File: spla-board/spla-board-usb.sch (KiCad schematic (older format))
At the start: 22 parts, among them J1 USB_B_Micro, U2 FT2232H, U3 93LC66B, X1 O252012MEDH4MI

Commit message: schematic: Add Digikey and ManufacturerId fields to big components.
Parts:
- U2: Digikey (none) -> 768-1024-1-ND; Manufacturer Id (none) -> FT2232HL
- U3: Digikey (none) -> 93LC66B/SN-ND; Manufacturer Id (none) -> 93LC66B/SN
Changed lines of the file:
@@
 F 2 "Package_QFP:LQFP-64_10x10mm_P0.5mm" H 9950 5650 50  0001 C CNN
 F 3 "https://www.ftdichip.com/Support/Documents/DataSheets/ICs/DS_FT2232H.pdf" H 9950 5650 50  0001 C CNN
+F 4 "768-1024-1-ND" H 9950 5650 50  0001 C CNN "Digikey"
+F 5 "FT2232HL" H 9950 5650 50  0001 C CNN "Manufacturer Id"
 	1    9950 5650
 	1    0    0    -1
@@
 F 2 "Package_SO:SOIC-8_3.9x4.9mm_P1.27mm" H 5700 6550 50  0001 C CNN
 F 3 "http://ww1.microchip.com/downloads/en/DeviceDoc/20001749K.pdf" H 5700 6550 50  0001 C CNN
+F 4 "93LC66B/SN-ND" H 5700 6550 50  0001 C CNN "Digikey"
+F 5 "93LC66B/SN" H 5700 6550 50  0001 C CNN "Manufacturer Id"
 	1    5700 6550
 	1    0    0    -1

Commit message: schematic: Select LED part.
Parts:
- D3, D4: Digikey (none) -> 732-4986-1-ND; Manufacturer Id (none) -> 150080VS75000
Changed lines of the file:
@@
 F 2 "LED_SMD:LED_0805_2012Metric" H 12400 6700 50  0001 C CNN
 F 3 "~" H 12400 6700 50  0001 C CNN
+F 4 "732-4986-1-ND" H 12400 6700 50  0001 C CNN "Digikey"
+F 5 "150080VS75000" H 12400 6700 50  0001 C CNN "Manufacturer Id"
 	1    12400 6700
 	0    -1   -1   0
@@
 F 2 "LED_SMD:LED_0805_2012Metric" H 12400 5600 50  0001 C CNN
 F 3 "~" H 12400 5600 50  0001 C CNN
+F 4 "732-4986-1-ND" H 12400 5600 50  0001 C CNN "Digikey"
+F 5 "150080VS75000" H 12400 5600 50  0001 C CNN "Manufacturer Id"
 	1    12400 5600
 	0    -1   -1   0

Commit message: schematic: Add part numbers for USB and power jack.
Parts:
- J1: Digikey (none) -> 732-5960-1-ND; Manufacturer Id (none) -> 629105150521
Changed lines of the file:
@@
 F 2 "Connector_USB:USB_Micro-B_Wuerth_629105150521" H 2950 4800 50  0001 C CNN
 F 3 "~" H 2950 4800 50  0001 C CNN
+F 4 "732-5960-1-ND" H 2800 4850 50  0001 C CNN "Digikey"
+F 5 "629105150521" H 2800 4850 50  0001 C CNN "Manufacturer Id"
 	1    2800 4850
 	1    0    0    1

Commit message: schematic: Lower-case 'k' in resistors.
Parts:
- R2, R4, R5: value 10K -> 10k
- R3: value 2.2K -> 2.2k
- R6: value 12K -> 12k
- R7: value 1K -> 1k
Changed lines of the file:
@@
 P 6800 6850
 F 0 "R3" V 6595 6850 50  0000 C CNN
-F 1 "2.2K" V 6686 6850 50  0000 C CNN
+F 1 "2.2k" V 6686 6850 50  0000 C CNN
 F 2 "Resistor_SMD:R_0603_1608Metric" V 6840 6840 50  0001 C CNN
 F 3 "~" H 6800 6850 50  0001 C CNN
@@
 P 6400 5600
 F 0 "R2" H 6468 5646 50  0000 L CNN
-F 1 "10K" H 6468 5555 50  0000 L CNN
+F 1 "10k" H 6468 5555 50  0000 L CNN
 F 2 "Resistor_SMD:R_0603_1608Metric" V 6440 5590 50  0001 C CNN
 F 3 "~" H 6400 5600 50  0001 C CNN
@@
 P 6850 5600
 F 0 "R4" H 6918 5646 50  0000 L CNN
-F 1 "10K" H 6918 5555 50  0000 L CNN
+F 1 "10k" H 6918 5555 50  0000 L CNN
 F 2 "Resistor_SMD:R_0603_1608Metric" V 6890 5590 50  0001 C CNN
 F 3 "~" H 6850 5600 50  0001 C CNN
@@
 P 7250 5600
 F 0 "R5" H 7318 5646 50  0000 L CNN
-F 1 "10K" H 7318 5555 50  0000 L CNN
+F 1 "10k" H 7318 5555 50  0000 L CNN
 F 2 "Resistor_SMD:R_0603_1608Metric" V 7290 5590 50  0001 C CNN
 F 3 "~" H 7250 5600 50  0001 C CNN
@@
 P 7800 5250
 F 0 "R6" H 7868 5296 50  0000 L CNN
-F 1 "12K" H 7868 5205 50  0000 L CNN
+F 1 "12k" H 7868 5205 50  0000 L CNN
 F 2 "Resistor_SMD:R_0603_1608Metric" V 7840 5240 50  0001 C CNN
 F 3 "~" H 7800 5250 50  0001 C CNN
@@
 P 8300 5600
 F 0 "R7" H 8368 5646 50  0000 L CNN
-F 1 "1K" H 8368 5555 50  0000 L CNN
+F 1 "1k" H 8368 5555 50  0000 L CNN
 F 2 "Resistor_SMD:R_0603_1608Metric" V 8340 5590 50  0001 C CNN
 F 3 "~" H 8300 5600 50  0001 C CNN

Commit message: schematic/pcb: Swap oscillator for FOX924 equivalent.
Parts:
- X1: value O252012MEDH4MI -> FT5HNBPK12.0-T1; footprint Crystal:Crystal_SMD_2520-4Pin_2.5x2.0mm -> Crystal:Crystal_SMD_5032-4Pin_5.0x3.2mm; symbol SPLA:O252012MEDH4MI -> SPLA:FT5HNBPK12.0-T1; Digikey (none) -> 631-1068-1-ND; Manufacturer Id (none) -> FT5HNBPK12.0-T1
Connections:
- no-connect marks 7 -> 8
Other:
- note removed: "CMOS digital oscillator, rather than FTDI's crystal suggestion"
- moved on the sheet: C2
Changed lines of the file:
@@
 L Device:C_Small C2
 U 1 1 5E53DEA7
-P 6350 7600
-F 0 "C2" H 6465 7646 50  0000 L CNN
-F 1 "0.1uF" H 6465 7555 50  0000 L CNN
-F 2 "Capacitor_SMD:C_0603_1608Metric" H 6388 7450 50  0001 C CNN
-F 3 "~" H 6350 7600 50  0001 C CNN
-	1    6350 7600
+P 6350 7700
+F 0 "C2" H 6465 7746 50  0000 L CNN
+F 1 "0.1uF" H 6465 7655 50  0000 L CNN
+F 2 "Capacitor_SMD:C_0603_1608Metric" H 6388 7550 50  0001 C CNN
+F 3 "~" H 6350 7700 50  0001 C CNN
+	1    6350 7700
 	1    0    0    -1
 $EndComp
@@
 L power:GND #PWR0105
 U 1 1 5E58FEB5
-P 6350 7900
-F 0 "#PWR0105" H 6350 7650 50  0001 C CNN
-F 1 "GND" H 6355 7727 50  0000 C CNN
-F 2 "" H 6350 7900 50  0001 C CNN
-F 3 "" H 6350 7900 50  0001 C CNN
-	1    6350 7900
+P 6350 8000
+F 0 "#PWR0105" H 6350 7750 50  0001 C CNN
+F 1 "GND" H 6355 7827 50  0000 C CNN
+F 2 "" H 6350 8000 50  0001 C CNN
+F 3 "" H 6350 8000 50  0001 C CNN
+	1    6350 8000
 	1    0    0    -1
 $EndComp
@@
 L power:+3V3 #PWR0109
 U 1 1 5E649611
-P 7550 7350
-F 0 "#PWR0109" H 7550 7200 50  0001 C CNN
-F 1 "+3V3" H 7565 7523 50  0000 C CNN
-F 2 "" H 7550 7350 50  0001 C CNN
-F 3 "" H 7550 7350 50  0001 C CNN
-	1    7550 7350
+P 6350 7350
+F 0 "#PWR0109" H 6350 7200 50  0001 C CNN
+F 1 "+3V3" H 6365 7523 50  0000 C CNN
+F 2 "" H 6350 7350 50  0001 C CNN
+F 3 "" H 6350 7350 50  0001 C CNN
+	1    6350 7350
 	1    0    0    -1
 $EndComp
@@
 FIFO_SIWU
 $Comp
-L SPLA:O252012MEDH4MI X1
+L SPLA:FT5HNBPK12.0-T1 X1
 U 1 1 5FDCFC82
 P 7150 7800
+AR Path="/5FDCFC82" Ref="X1"  Part="1"
+AR Path="/5E4F712F/5FDCFC82" Ref="X1"  Part="1"
 F 0 "X1" H 6850 8050 50  0000 L CNN
-F 1 "O252012MEDH4MI" H 7150 7550 50  0000 C CNN
-F 2 "Crystal:Crystal_SMD_2520-4Pin_2.5x2.0mm" H 7200 7300 50  0001 C CNN
+F 1 "FT5HNBPK12.0-T1" H 7150 7550 50  0000 C CNN
+F 2 "Crystal:Crystal_SMD_5032-4Pin_5.0x3.2mm" H 7200 7300 50  0001 C CNN
 F 3 "" H 7580 7490 50  0001 C CNN
+F 4 "631-1068-1-ND" H 7150 7800 50  0001 C CNN "Digikey"
+F 5 "FT5HNBPK12.0-T1" H 7150 7800 50  0001 C CNN "Manufacturer Id"
 	1    7150 7800
 	1    0    0    -1
@@
 	6750 7900 6350 7900
 Wire Wire Line
-	6350 7350 6750 7350
-Wire Wire Line
-	7550 7700 7550 7350
-Connection ~ 7550 7350
-Wire Wire Line
-	6750 7700 6750 7350
-Connection ~ 6750 7350
-Wire Wire Line
-	6750 7350 7550 7350
+	7550 7700 7550 7450
 Connection ~ 6350 7900
 NoConn ~ 11150 5050
@@
 Connection ~ 8100 7900
 Wire Wire Line
-	6350 7350 6350 7500
-Wire Wire Line
-	6350 7700 6350 7900
-Text Notes 5400 8450 0    50   ~ 0
-CMOS digital oscillator, rather than FTDI's crystal suggestion
+	6350 7450 6350 7600
+Wire Wire Line
+	6350 7800 6350 7900
 Text GLabel 11150 7350 2    39   Output ~ 0
 USB_~PWREN~
@@
 Wire Wire Line
 	12400 6150 11150 6150
+Wire Wire Line
+	6350 7450 7550 7450
+NoConn ~ 6750 7700
+Connection ~ 6350 7450
+Wire Wire Line
+	6350 7450 6350 7350
+Wire Wire Line
+	6350 7900 6350 8000
 $EndSCHEMATC

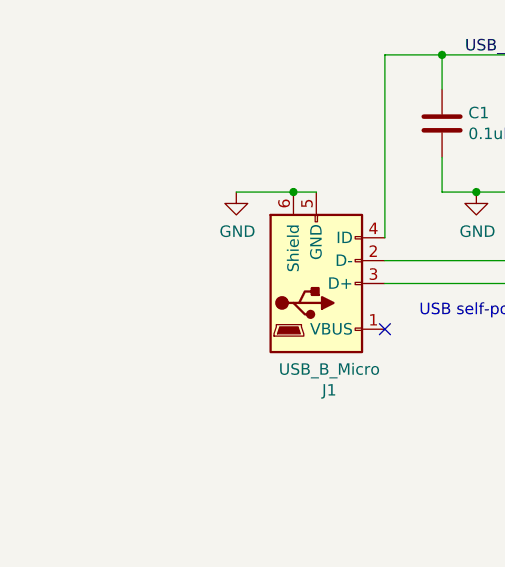
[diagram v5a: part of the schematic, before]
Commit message: schematic/pcb: Add BoM-only symbols.
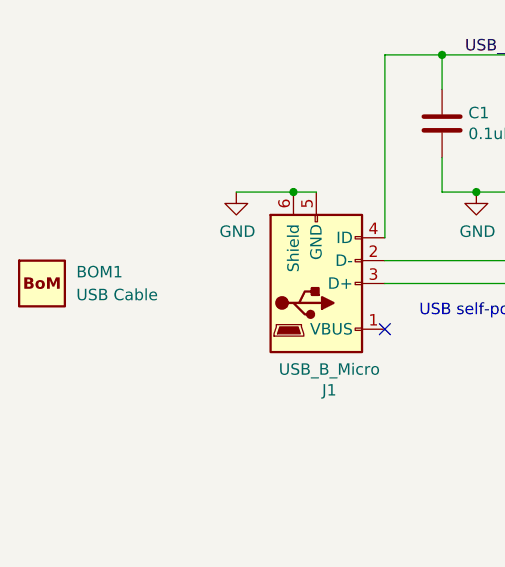
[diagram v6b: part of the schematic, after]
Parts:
- added BOM1: USB Cable, SPLA:BoM, symbol SPLA:BomExtra
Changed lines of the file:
@@
 Wire Wire Line
 	6350 7900 6350 8000
+$Comp
+L SPLA:BomExtra BOM1
+U 1 1 5EA5FF9A
+P 1600 4850
+F 0 "BOM1" H 1750 4900 50  0000 L CNN
+F 1 "USB Cable" H 1750 4800 50  0000 L CNN
+F 2 "SPLA:BoM" H 1600 4850 50  0001 C CNN
+F 3 "" H 1600 4850 50  0001 C CNN
+F 4 "AE11229-ND" H 1600 4850 50  0001 C CNN "Digikey"
+F 5 "AK67421-0.3-VM" H 1600 4850 50  0001 C CNN "Manufacturer Id"
+	1    1600 4850
+	1    0    0    -1
+$EndComp
 $EndSCHEMATC

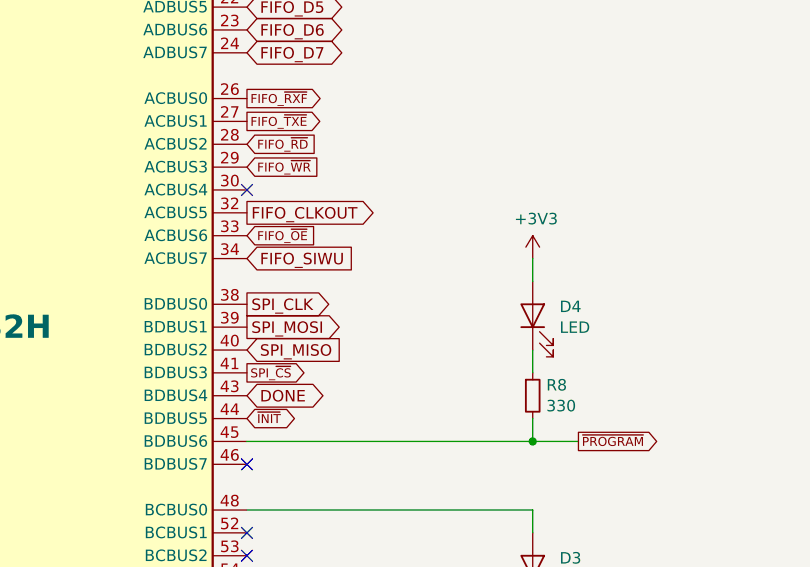
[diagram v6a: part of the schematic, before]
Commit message: schematic/pcb: Add pullup to SPI_CS and pulldown to PPU2_RESET.
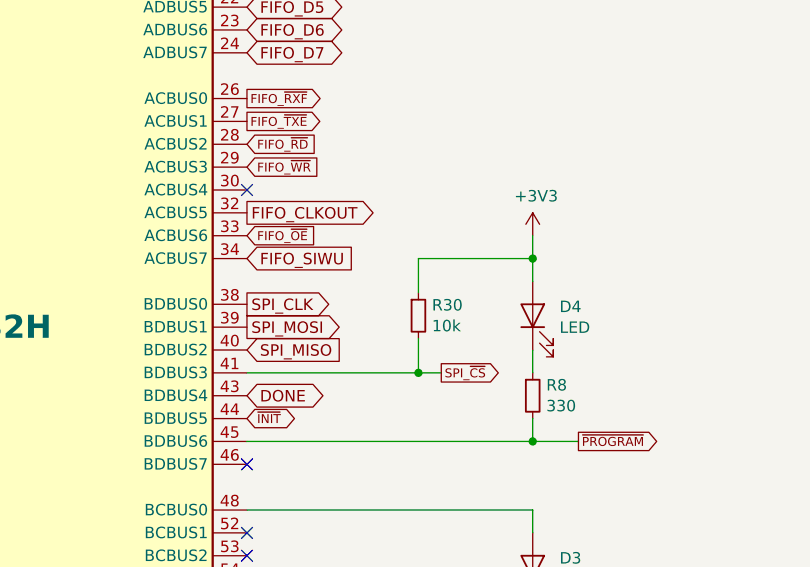
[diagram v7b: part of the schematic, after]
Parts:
- added R30: 10k, Resistor_SMD:R_0603_1608Metric, symbol Device:R_Small
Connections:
- net +3V3: now also R30.1
- net SPI_~CS~: now also R30.2
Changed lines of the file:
@@
 Text GLabel 11150 4450 2    50   BiDi ~ 0
 FIFO_D7
-Text GLabel 11150 5850 2    39   Output ~ 0
+Text GLabel 12000 5850 2    39   Output ~ 0
 SPI_~CS~
 Text GLabel 11150 4650 2    39   Output ~ 0
@@
 L power:+3V3 #PWR?
 U 1 1 5E9C89C1
-P 12400 5350
+P 12400 5250
 AR Path="/5E4D8358/5E9C89C1" Ref="#PWR?"  Part="1"
 AR Path="/5E4F712F/5E9C89C1" Ref="#PWR053"  Part="1"
-F 0 "#PWR053" H 12400 5200 50  0001 C CNN
-F 1 "+3V3" H 12415 5523 50  0000 C CNN
-F 2 "" H 12400 5350 50  0001 C CNN
-F 3 "" H 12400 5350 50  0001 C CNN
-	1    12400 5350
-	1    0    0    -1
-$EndComp
-Wire Wire Line
-	12400 5350 12400 5450
+F 0 "#PWR053" H 12400 5100 50  0001 C CNN
+F 1 "+3V3" H 12415 5423 50  0000 C CNN
+F 2 "" H 12400 5250 50  0001 C CNN
+F 3 "" H 12400 5250 50  0001 C CNN
+	1    12400 5250
+	1    0    0    -1
+$EndComp
+Wire Wire Line
+	12400 5250 12400 5350
 Wire Wire Line
 	12600 6150 12400 6150
@@
 	1    0    0    -1
 $EndComp
+Wire Wire Line
+	11150 5850 11900 5850
+Wire Wire Line
+	11900 5850 11900 5700
+Connection ~ 11900 5850
+Wire Wire Line
+	11900 5850 12000 5850
+$Comp
+L Device:R_Small R30
+U 1 1 5EB42683
+P 11900 5600
+F 0 "R30" H 11959 5646 50  0000 L CNN
+F 1 "10k" H 11959 5555 50  0000 L CNN
+F 2 "Resistor_SMD:R_0603_1608Metric" H 11900 5600 50  0001 C CNN
+F 3 "~" H 11900 5600 50  0001 C CNN
+	1    11900 5600
+	1    0    0    -1
+$EndComp
+Wire Wire Line
+	12400 5350 11900 5350
+Wire Wire Line
+	11900 5350 11900 5500
+Connection ~ 12400 5350
+Wire Wire Line
+	12400 5350 12400 5450
 $EndSCHEMATC

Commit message: bom: Add manufacturers.
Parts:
- BOM1: Manufacturer (none) -> Assmann WSW Components
- D3, D4, J1: Manufacturer (none) -> Wuerth Electronik
- U2: Manufacturer (none) -> FTDI Ltd.
- U3: Manufacturer (none) -> Microchip Technology
- X1: Manufacturer (none) -> Fox Electronics
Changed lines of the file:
@@
 F 4 "768-1024-1-ND" H 9950 5650 50  0001 C CNN "Digikey"
 F 5 "FT2232HL" H 9950 5650 50  0001 C CNN "Manufacturer Id"
+F 6 "FTDI Ltd." H 9950 5650 50  0001 C CNN "Manufacturer"
 	1    9950 5650
 	1    0    0    -1
@@
 F 4 "732-5960-1-ND" H 2800 4850 50  0001 C CNN "Digikey"
 F 5 "629105150521" H 2800 4850 50  0001 C CNN "Manufacturer Id"
+F 6 "Wuerth Electronik" H 2800 4850 50  0001 C CNN "Manufacturer"
 	1    2800 4850
 	1    0    0    1
@@
 F 4 "631-1068-1-ND" H 7150 7800 50  0001 C CNN "Digikey"
 F 5 "FT5HNBPK12.0-T1" H 7150 7800 50  0001 C CNN "Manufacturer Id"
+F 6 "Fox Electronics" H 7150 7800 50  0001 C CNN "Manufacturer"
 	1    7150 7800
 	1    0    0    -1
@@
 F 4 "732-4986-1-ND" H 12400 6700 50  0001 C CNN "Digikey"
 F 5 "150080VS75000" H 12400 6700 50  0001 C CNN "Manufacturer Id"
+F 6 "Wuerth Electronik" H 12400 6700 50  0001 C CNN "Manufacturer"
 	1    12400 6700
 	0    -1   -1   0
@@
 F 4 "93LC66B/SN-ND" H 5700 6550 50  0001 C CNN "Digikey"
 F 5 "93LC66B/SN" H 5700 6550 50  0001 C CNN "Manufacturer Id"
+F 6 "Microchip Technology" H 5700 6550 50  0001 C CNN "Manufacturer"
 	1    5700 6550
 	1    0    0    -1
@@
 F 4 "732-4986-1-ND" H 12400 5600 50  0001 C CNN "Digikey"
 F 5 "150080VS75000" H 12400 5600 50  0001 C CNN "Manufacturer Id"
+F 6 "Wuerth Electronik" H 12400 5600 50  0001 C CNN "Manufacturer"
 	1    12400 5600
 	0    -1   -1   0
@@
 F 4 "AE11229-ND" H 1600 4850 50  0001 C CNN "Digikey"
 F 5 "AK67421-0.3-VM" H 1600 4850 50  0001 C CNN "Manufacturer Id"
+F 6 "Assmann WSW Components" H 1600 4850 50  0001 C CNN "Manufacturer"
 	1    1600 4850
 	1    0    0    -1
